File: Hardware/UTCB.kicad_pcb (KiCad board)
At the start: 2 copper layers, 236 parts, among them J1 NR01105ANG13-2C, J10 Conn_01x06, J2 NR01105ANG13-2C, J3 NR01105ANG13-2C, J4 NR01105ANG13-2C, J5 NR01105ANG13-2C, J6 NR01105ANG13-2C, J7 VXO7805-500-M-TR, J8 3557-2, J9 Conn_01x02, Q1 2SD2653KT146, Q10 2SD2653KT146, Q11 2SD2653KT146, Q12 2SD2653KT146, Q13 2SD2653KT146, Q14 2SD2653KT146, Q15 2SD2653KT146, Q16 2SD2653KT146, Q17 2SD2653KT146, Q18 2SD2653KT146, Q19 2SD2653KT146, Q2 2SD2653KT146, Q20 2SD2653KT146, Q21 2SD2653KT146, Q22 2SD2653KT146, Q23 2SD2653KT146, Q24 2SD2653KT146, Q25 2SD2653KT146, Q26 2SD2653KT146, Q27 2SD2653KT146, Q28 2SD2653KT146, Q29 2SD2653KT146, Q3 2SD2653KT146, Q30 2SD2653KT146, Q31 2SD2653KT146, Q32 2SD2653KT146, Q33 2SD2653KT146, Q34 2SD2653KT146, Q35 2SD2653KT146, Q36 2SD2653KT146, Q37 2SD2653KT146, Q38 2SD2653KT146, Q39 2SD2653KT146, Q4 2SD2653KT146, Q40 2SD2653KT146, Q41 2SD2653KT146, Q42 2SD2653KT146, Q43 2SD2653KT146, Q44 2SD2653KT146, Q45 2SD2653KT146, Q46 2SD2653KT146, Q47 2SD2653KT146, Q48 2SD2653KT146, Q5 2SD2653KT146, Q6 2SD2653KT146, Q7 2SD2653KT146, Q8 2SD2653KT146, Q9 2SD2653KT146

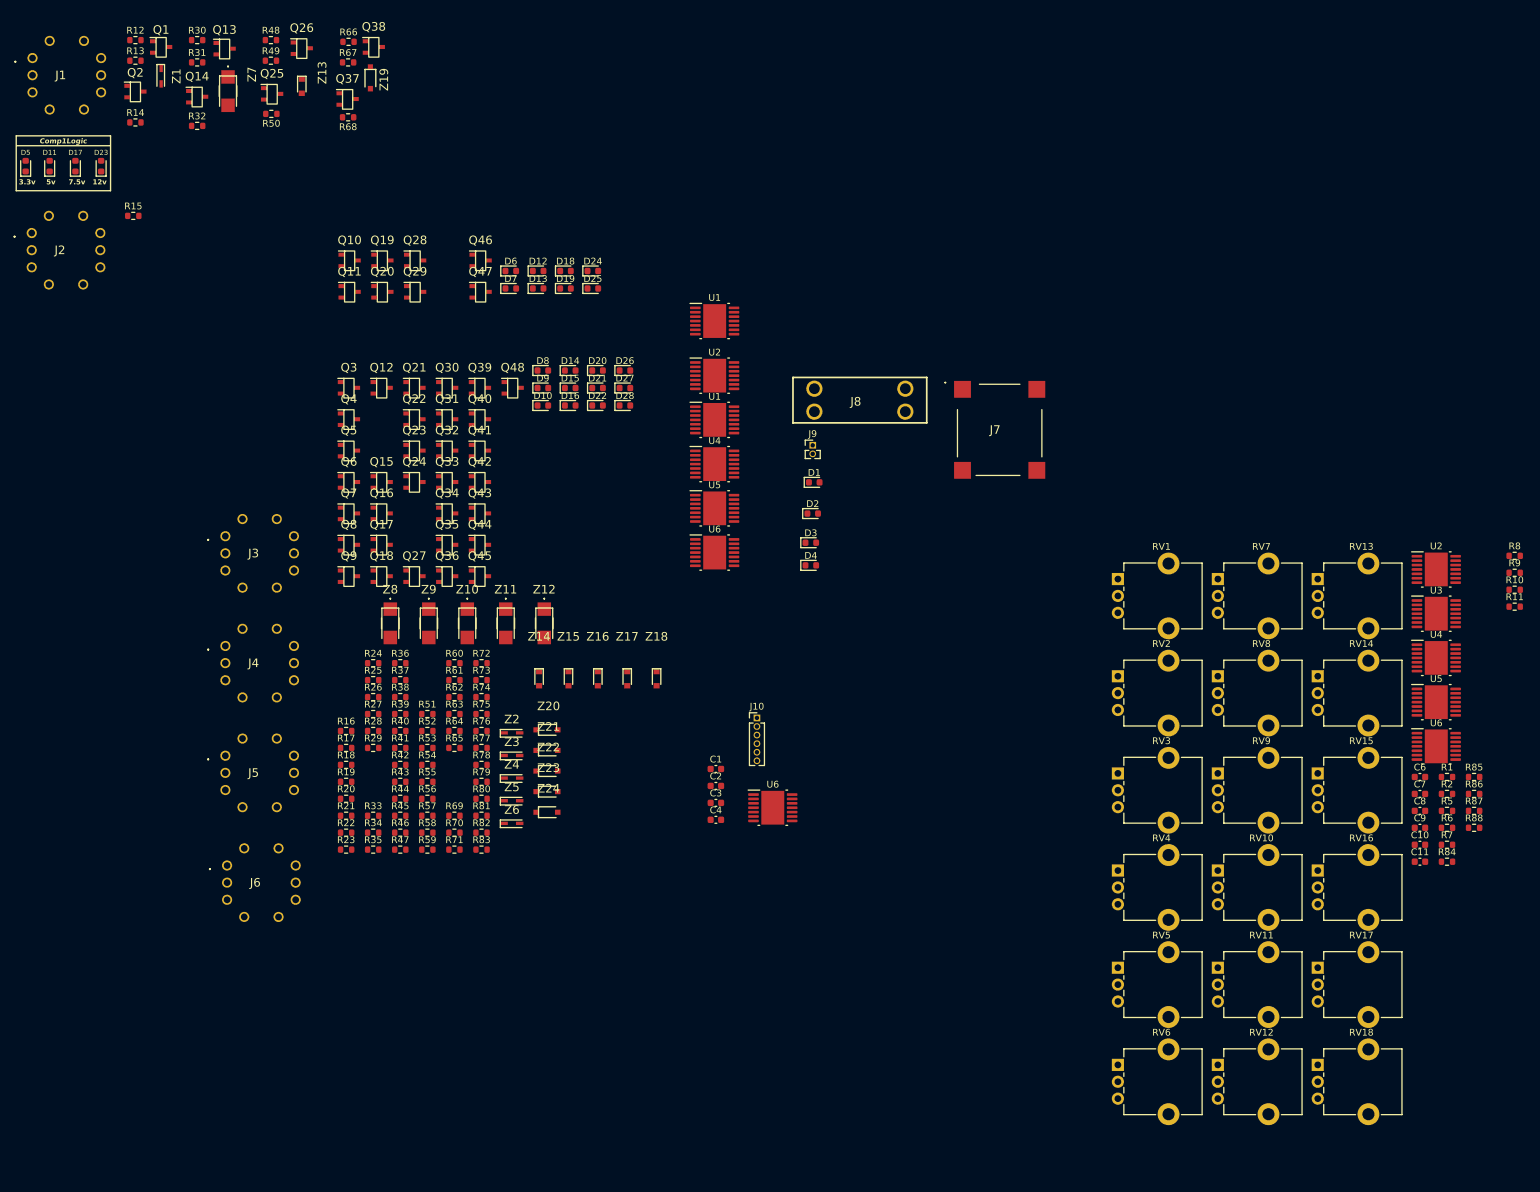
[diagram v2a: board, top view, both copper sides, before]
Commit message: Added changes to logic side for comparator inputs
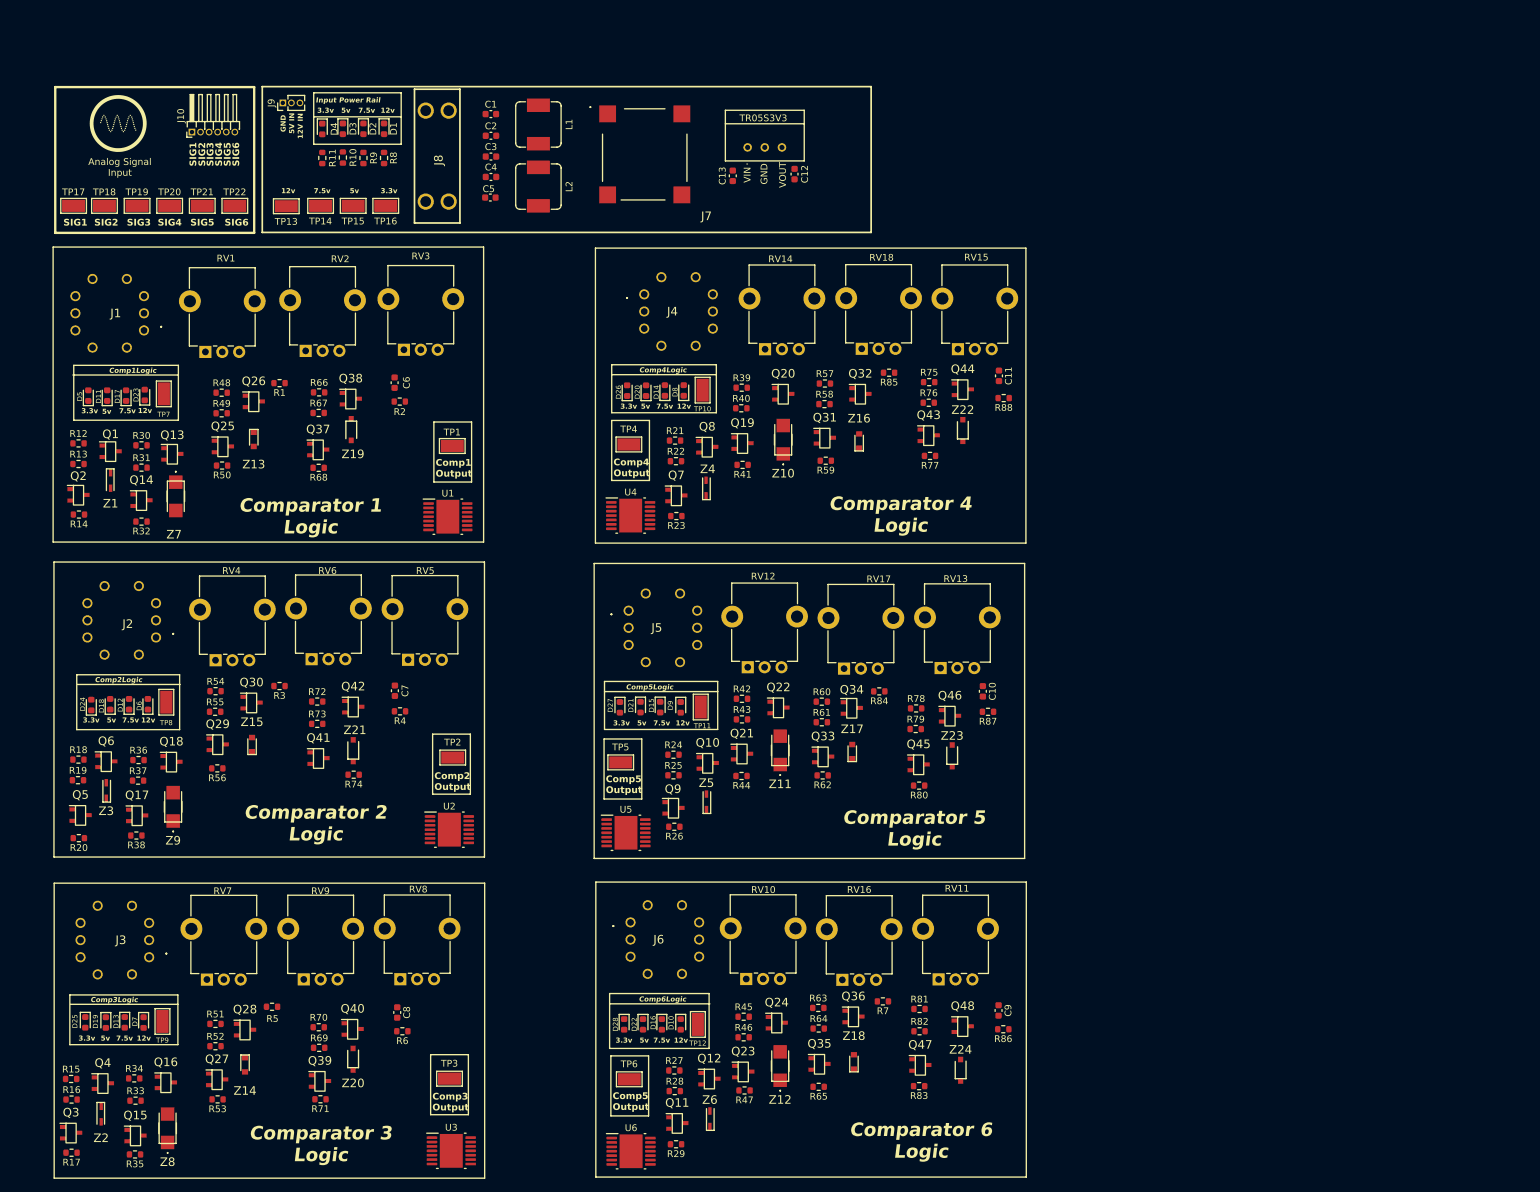
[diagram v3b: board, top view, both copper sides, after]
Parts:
- removed the U1 at (119.1, 72.1)
- removed the U1 at (119.1, 57.5)
- removed the U2 at (225.9, 94.3)
- removed the U4 at (119.1, 78.7)
- removed the U5 at (119.1, 85.2)
- removed the U6 at (127.7, 129.6)
- removed the U6 at (119.1, 91.8)
- added C12: 47uF, Capacitor_SMD:C_0603_1608Metric, F.Cu at (130.9, 35.7)
- added C13: 22uF, Capacitor_SMD:C_0603_1608Metric, F.Cu at (121.7, 36.0)
- added C5: C_Small, Capacitor_SMD:C_0603_1608Metric, F.Cu at (85.8, 39.2)
- added G***: LOGO, Symbol:AnalogSymbolIcon, F.Cu at (30.7, 28.2)
- added IC1: TR05S3V3, Converter_DCDC:TR05S3V3, F.Cu at (126.5, 33.8)
- added L1: 82uH, Inductor_SMD:L_Sumida_CDMC6D28_7.25x6.5mm, F.Cu at (93.0, 28.4)
- added L2: 22uH, Inductor_SMD:L_Sumida_CDMC6D28_7.25x6.5mm, F.Cu at (93.0, 37.6)
- added R3: 10kΩ, Resistor_SMD:R_0603_1608Metric, F.Cu at (54.6, 111.5)
- added R4: 10kΩ, Resistor_SMD:R_0603_1608Metric, F.Cu at (72.5, 115.3)
- added TP1: Comp1_Output, TestPoint:TestPoint_Keystone_5015_Micro-Minature, F.Cu at (80.2, 76.0)
- added TP10: Comp4_Logic, TestPoint:TestPoint_Keystone_5015_Micro-Minature, F.Cu at (117.3, 67.7)
- added TP11: Comp5_Logic, TestPoint:TestPoint_Keystone_5015_Micro-Minature, F.Cu at (117.0, 114.6)
- added TP12: Comp6_Logic, TestPoint:TestPoint_Keystone_5015_Micro-Minature, F.Cu at (116.6, 161.7)
- added TP13: 12v_Check, TestPoint:TestPoint_Keystone_5015_Micro-Minature, F.Cu at (55.6, 40.5)
- added TP14: 7.5v_Check, TestPoint:TestPoint_Keystone_5015_Micro-Minature, F.Cu at (60.7, 40.4)
- added TP15: 5v_Check, TestPoint:TestPoint_Keystone_5015_Micro-Minature, F.Cu at (65.5, 40.4)
- added TP16: 3.3v_Check, TestPoint:TestPoint_Keystone_5015_Micro-Minature, F.Cu at (70.3, 40.4)
- added TP17: Signal1_Check, TestPoint:TestPoint_Keystone_5015_Micro-Minature, F.Cu at (24.1, 40.4)
- added TP18: Signal2_Check, TestPoint:TestPoint_Keystone_5015_Micro-Minature, F.Cu at (28.7, 40.4)
- added TP19: Signal3_Check, TestPoint:TestPoint_Keystone_5015_Micro-Minature, F.Cu at (33.5, 40.4)
- added TP2: Comp2_Output, TestPoint:TestPoint_Keystone_5015_Micro-Minature, F.Cu at (80.3, 122.1)
- added TP20: Signal4_Check, TestPoint:TestPoint_Keystone_5015_Micro-Minature, F.Cu at (38.3, 40.4)
- added TP21: Signal5_Check, TestPoint:TestPoint_Keystone_5015_Micro-Minature, F.Cu at (43.2, 40.4)
- added TP22: Signal6_Check, TestPoint:TestPoint_Keystone_5015_Micro-Minature, F.Cu at (48.0, 40.4)
- added TP3: Comp3_Output, TestPoint:TestPoint_Keystone_5015_Micro-Minature, F.Cu at (79.8, 169.7)
- added TP4: Comp4_Output, TestPoint:TestPoint_Keystone_5015_Micro-Minature, F.Cu at (106.4, 75.8)
- added TP5: Comp5_Output, TestPoint:TestPoint_Keystone_5015_Micro-Minature, F.Cu at (105.1, 122.8)
- added TP6: Comp6_Output, TestPoint:TestPoint_Keystone_5015_Micro-Minature, F.Cu at (106.4, 169.8)
- added TP7: Comp1_Logic, TestPoint:TestPoint_Keystone_5015_Micro-Minature, F.Cu at (37.5, 68.3)
- added TP8: Comp2_Logic, TestPoint:TestPoint_Keystone_5015_Micro-Minature, F.Cu at (37.8, 113.9)
- added TP9: Comp3_Logic, TestPoint:TestPoint_Keystone_5015_Micro-Minature, F.Cu at (37.3, 161.2)
- added U1: ~, Package_SO:HTSSOP-14-1EP_4.4x5mm_P0.65mm_EP3.4x5mm_Mask3x3.1mm, F.Cu at (79.5, 86.5)
- J10: footprint Connector_PinHeader_1.27mm:PinHeader_1x06_P1.27mm_Vertical -> Connector_PinHeader_1.27mm:PinHeader_1x06_P1.27mm_Horizontal
- J9: value Conn_01x02 -> Conn_01x03; footprint Connector_PinHeader_1.27mm:PinHeader_1x02_P1.27mm_Vertical -> Connector_PinHeader_1.27mm:PinHeader_1x03_P1.27mm_Vertical
- moved R11 188.7 mm to (60.9, 33.3), turned to 90 degrees
- moved R10 185.0 mm to (64.0, 33.3), turned to -90 degrees
- moved R1 182.5 mm to (54.6, 66.7), turned to 180 degrees
- moved R9 181.2 mm to (67.0, 33.3), turned to -90 degrees
- moved R8 177.5 mm to (70.1, 33.3), turned to -90 degrees
- moved R5 176.4 mm to (53.5, 159.0), turned to 180 degrees
- moved U3 166.1 mm to (80.1, 180.4)
- moved R2 165.6 mm to (72.4, 69.4)
- moved C6 162.7 mm to (71.7, 66.6), turned to -90 degrees
- moved RV7 161.0 mm to (43.9, 155.0), turned to 90 degrees
- moved R6 157.6 mm to (72.8, 162.7), turned to 180 degrees
- moved C8 154.4 mm to (72.0, 159.9), turned to -90 degrees
- moved C7 152.6 mm to (71.7, 112.2), turned to -90 degrees
- moved RV1 139.3 mm to (43.6, 62.1), turned to 90 degrees
- moved RV9 138.8 mm to (58.2, 155.0), turned to 90 degrees
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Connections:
- J9 pad 1: +5V -> GND
- J9 pad 2: +12V -> +5V
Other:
- board text added: "12V IN"
- board text added: "5V IN"
- board text added: "Analog Signal Input"
- board text added: "Comp1 Output"
- board text added: "Comp2 Output"
- board text added: "Comp2Logic"
- board text added: "Comp3 Output"
- board text added: "Comp3Logic"
- board text added: "Comp4 Output"
- board text added: "Comp4Logic"
- board text added: "Comp5 Output"
- board text added: "Comp5Logic"
- board text added: "Comp6Logic"
- board text added: "Comparator 1 Logic"
- board text added: "Comparator 2 Logic"
- board text added: "Comparator 3 Logic"
- board text added: "Comparator 4 Logic"
- board text added: "Comparator 5 Logic"
- board text added: "Comparator 6 Logic"
- board text added: "GND"
- board text added: "Input Power Rail"
- board text added: "SIG1"
- board text added: "SIG2"
- board text added: "SIG3"
- board text added: "SIG4"
- board text added: "SIG5"
- board text added: "SIG6"
